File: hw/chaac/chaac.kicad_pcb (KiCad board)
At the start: 2 copper layers, 74.5 x 45.5 mm, 60 parts, among them J1 windrain, J2 AM2315, J3 Battery, J4 Solar Panel, J5 UART, Q1 Q_PMOS_GSD, SW1 RST, SW2 RST, U1 MIC550X, U2 CHAAC_RADIO, U3 BMP280, U4 MCP73871

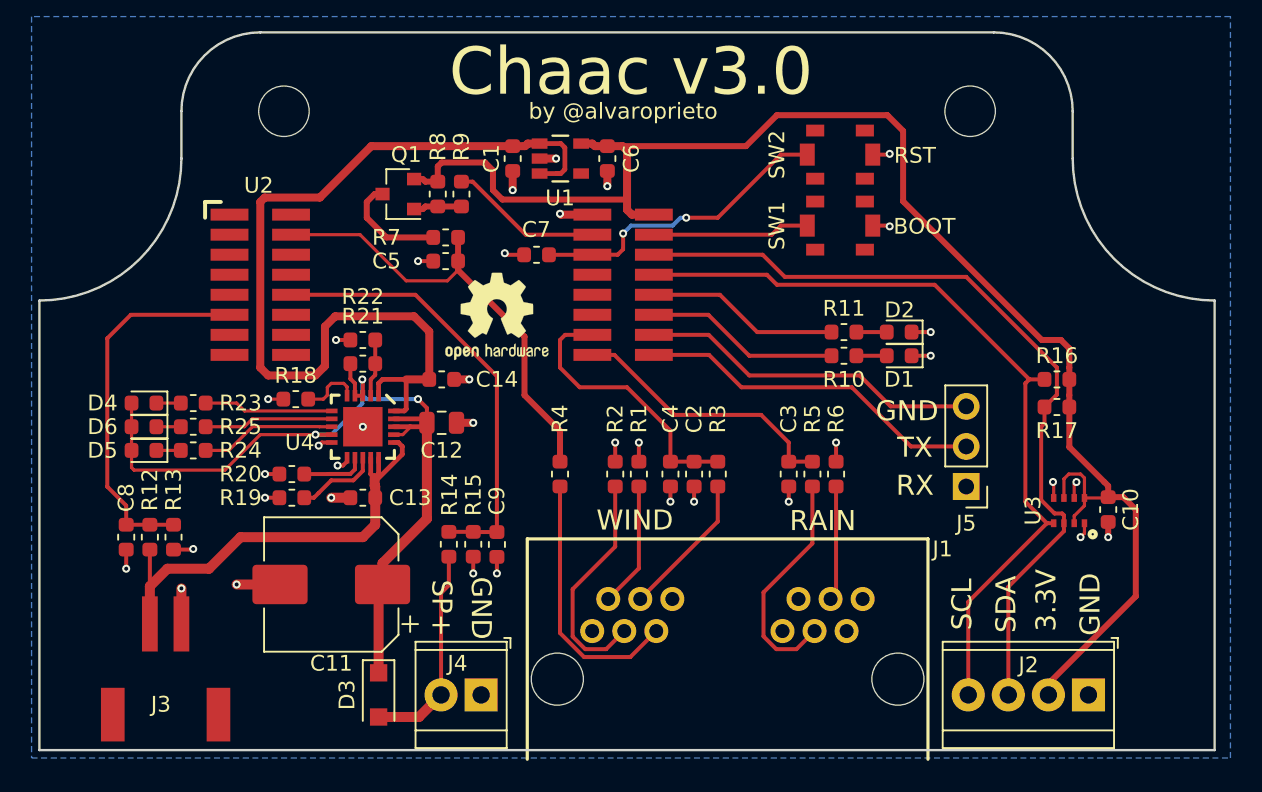
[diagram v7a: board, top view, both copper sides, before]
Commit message: Removed chaac radio from chaac and used 2 connectors
Ordered chaac radio from JLCPCB
Ordered chaac from oshpark
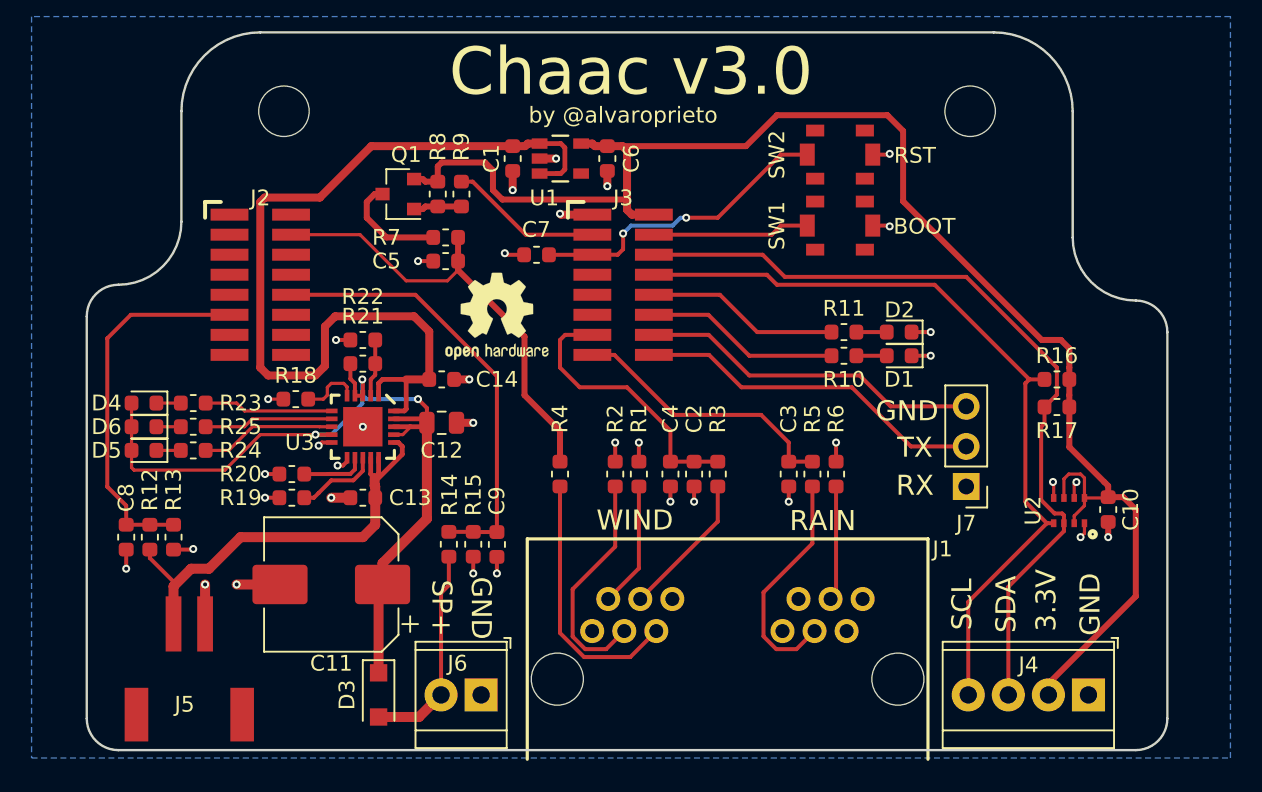
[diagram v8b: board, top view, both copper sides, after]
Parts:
- removed the U2 at (135.0, 91.0)
- added J2: Conn_02x08_Odd_Even, alvarop:20021121-00016C4LF, F.Cu at (123.5, 91.0)
- added J3: Conn_02x08_Odd_Even, alvarop:20021121-00016C4LF, F.Cu at (146.5, 91.0)
- moved J5 1.50 mm to (119.0, 112.5)
- renumbered J2 to J4, J3 to J5, J4 to J6, J5 to J7, U3 to U2, U4 to U3
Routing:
- net /VBATT: track 30.0 -> 29.1 mm
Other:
- board size 74.5 x 45.5 mm -> 68.5 x 45.5 mm
